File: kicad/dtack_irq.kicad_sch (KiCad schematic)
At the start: 14 parts, among them U12 GAL22V10, U13 GAL22V10

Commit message: - Added buffers for LED indicators in kicad - Removed pullups on FC0.2 in kicad - Connected FC0-2 to glue logic in kicad - Revamped glue logic for irg and iack in Digital
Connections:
- net ~{IACK6} is gone; now on net ~{IACK1}: U13.15 (I/O)
- net ~{IACK1}: no longer U13.19 (I/O)
- net ~{IACK2}: now also U13.16 (I/O); no longer U13.18 (I/O)
- net ~{IACK3}: now also U13.17 (I/O); no longer U13.21 (I/O)
- net ~{IACK4}: now also U13.18 (I/O); no longer U13.17 (I/O)
- net ~{IACK5}: now also U13.19 (I/O), U13.20 (I/O); no longer U13.16 (I/O)
- net ~{IACK7}: now also U13.21 (I/O); no longer U13.14 (I/O)
- no-connect marks 0 -> 14
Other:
- note added: "Pin 14 is IACK0. Never connect to ground!"
- title: (none) -> Mats Brorson 68010 SBC DTACK and IRQ
- moved on the sheet: JP1, R8, R?, U12, U13

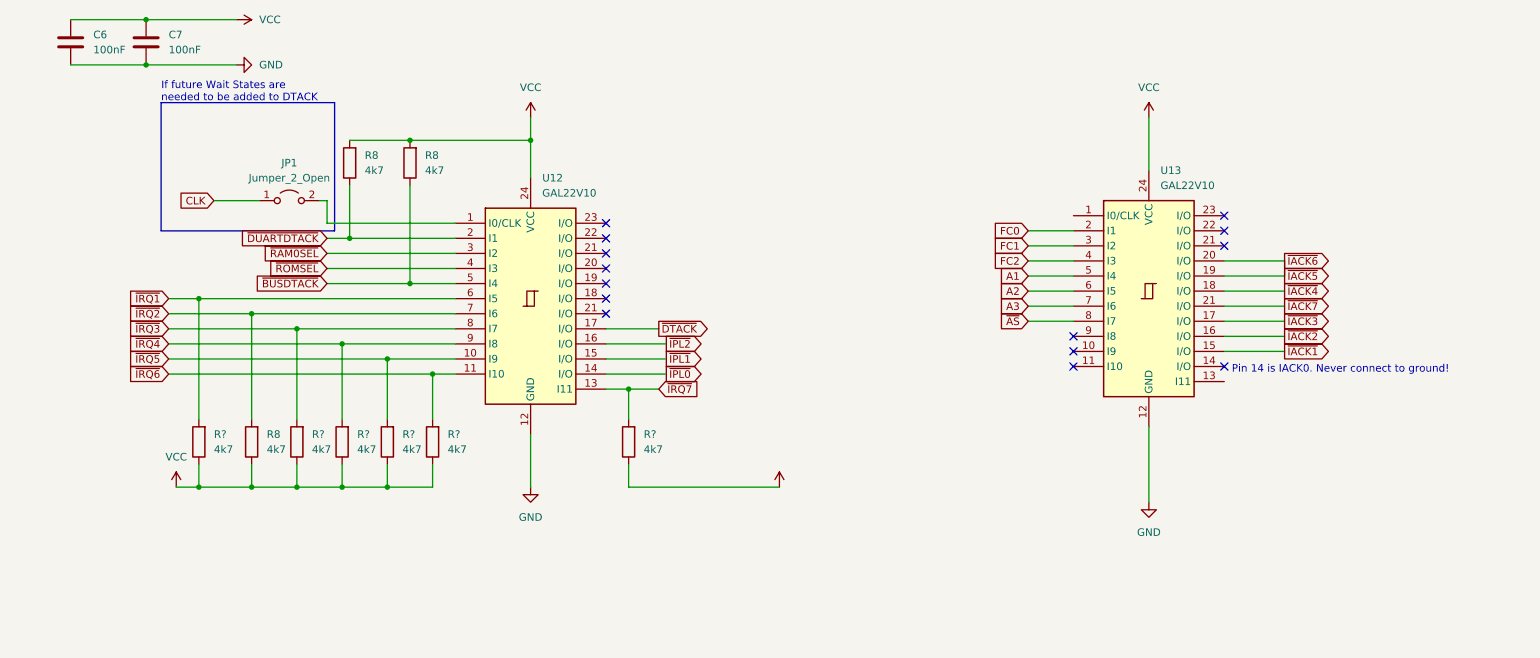
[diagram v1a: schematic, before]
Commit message: New decoding and GALs
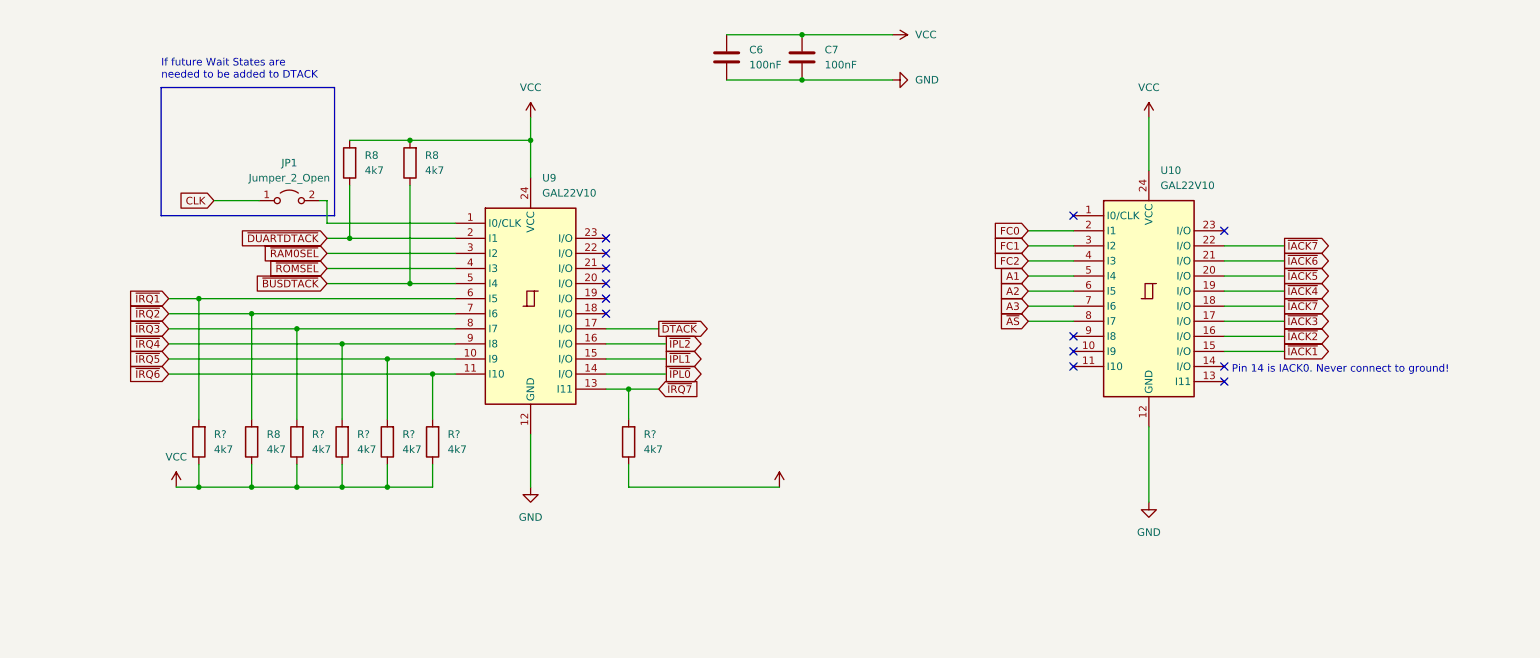
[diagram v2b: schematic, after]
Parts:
- removed U12, U13: GAL22V10, symbol Lattice_GAL_sym:GAL22V10
- added U10, U9: GAL22V10, symbol Lattice_GAL_sym:GAL22V10
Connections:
- net A1: now also U10.5 (I4)
- net A2: now also U10.6 (I5)
- net A3: now also U10.7 (I6)
- net FC0: now also U10.2 (I1)
- net FC1: now also U10.3 (I2)
- net FC2: now also U10.4 (I3)
- net GND: now also U10.12 (GND), U9.12 (GND)
- net VCC: now also U10.24 (VCC), U9.24 (VCC)
- net ~{AS}: now also U10.8 (I7)
- net ~{BUSDTACK}: now also U9.5 (I4)
- net ~{DTACK}: now also U9.17 (I/O)
- net ~{DUARTDTACK}: now also U9.2 (I1)
- net ~{IACK1}: now also U10.15 (I/O)
- net ~{IACK2}: now also U10.16 (I/O)
- net ~{IACK3}: now also U10.17 (I/O)
- net ~{IACK4}: now also U10.19 (I/O)
- net ~{IACK5}: now also U10.20 (I/O)
- net ~{IACK7}: now also U10.18 (I/O), U10.22 (I/O)
- net ~{IPL0}: now also U9.14 (I/O)
- net ~{IPL1}: now also U9.15 (I/O)
- net ~{IPL2}: now also U9.16 (I/O)
- net ~{IRQ1}: now also U9.6 (I5)
- net ~{IRQ2}: now also U9.7 (I6)
- net ~{IRQ3}: now also U9.8 (I7)
- net ~{IRQ4}: now also U9.9 (I8)
- net ~{IRQ5}: now also U9.10 (I9)
- net ~{IRQ6}: now also U9.11 (I10)
- net ~{IRQ7}: now also U9.13 (I11)
- net ~{RAM0SEL}: now also U9.3 (I2)
- net ~{ROMSEL}: now also U9.4 (I3)
- net at JP1.2 (B): now also U9.1 (I0/CLK)
- new net ~{IACK6}: U10.21 (I/O)
- no-connect marks 14 -> 13
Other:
- moved on the sheet: C6, C7

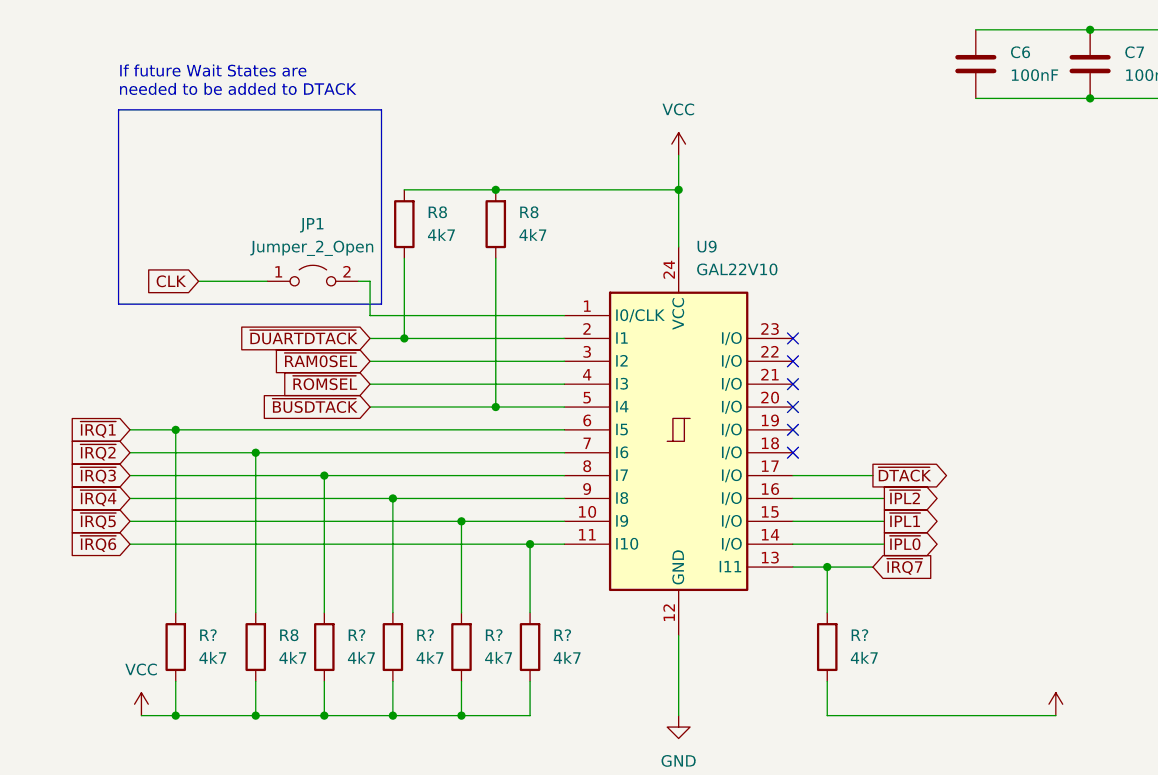
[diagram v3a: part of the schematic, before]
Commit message: switched to GALasm
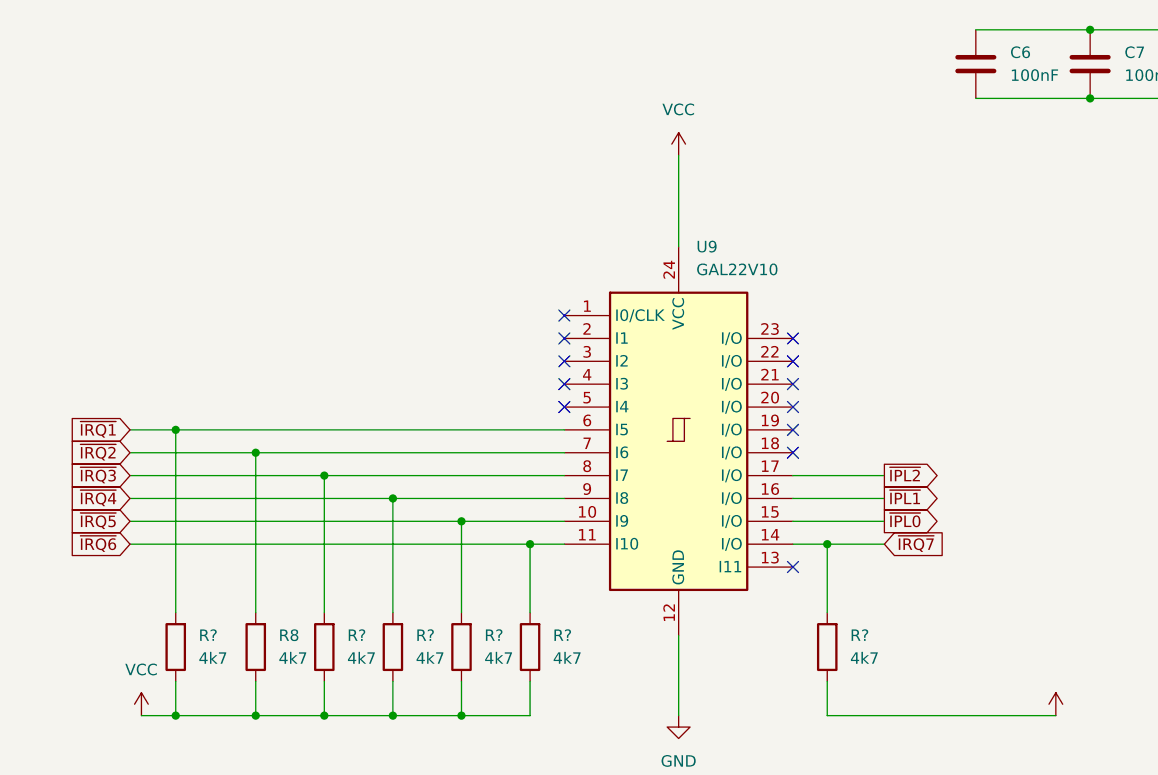
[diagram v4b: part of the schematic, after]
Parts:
- removed JP1: Jumper_2_Open, symbol Jumper:Jumper_2_Open
- removed R8 (x2): 4k7, Resistor_THT:R_Axial_DIN0207_L6.3mm_D2.5mm_P10.16mm_Horizontal, symbol Device:R
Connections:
- net ~{DTACK} is gone; now on net ~{IPL2}: U9.17 (I/O)
- net ~{IPL0}: now also U9.15 (I/O); no longer U9.14 (I/O)
- net ~{IPL1}: now also U9.16 (I/O); no longer U9.15 (I/O)
- net ~{IPL2}: no longer U9.16 (I/O)
- net ~{IRQ7}: now also U9.14 (I/O); no longer U9.13 (I11)
- net ~{BUSDTACK}: no longer names the net of U9.5 (I4)
- net ~{DUARTDTACK}: no longer names the net of U9.2 (I1)
- net ~{RAM0SEL}: no longer names the net of U9.3 (I2)
- net ~{ROMSEL}: no longer names the net of U9.4 (I3)
- no-connect marks 13 -> 19
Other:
- note removed: "If future Wait States are needed to be added to DTACK"

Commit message: finalized signaling PLD
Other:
- title: Mats Brorson 68010 SBC DTACK and IRQ -> Mats Brorson 68010 SBC IACK and IRQ
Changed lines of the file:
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@@
   (paper "A4")
   (title_block
-    (title "Mats Brorson 68010 SBC DTACK and IRQ")
+    (title "Mats Brorson 68010 SBC IACK and IRQ")
     (date "2023-12-28")
     (rev "1.0-alpha")

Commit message: added footprints
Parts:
- added J10, J14, J15, J9: Free pin, Connector_PinSocket_2.54mm:PinSocket_1x01_P2.54mm_Vertical, symbol Connector:Conn_01x01_Pin
- added J11: Free Pins, Connector_PinSocket_2.54mm:PinSocket_1x05_P2.54mm_Vertical, symbol Connector:Conn_01x05_Pin
- added J12: Free pins, Connector_PinSocket_2.54mm:PinSocket_1x06_P2.54mm_Vertical, symbol Connector:Conn_01x06_Pin
- added J13: Free pins, Connector_PinSocket_2.54mm:PinSocket_1x03_P2.54mm_Vertical, symbol Connector:Conn_01x03_Pin
- U16: renamed from U10; footprint (none) -> Package_DIP:DIP-24_W7.62mm_Socket
- U17: renamed from U9; footprint (none) -> Package_DIP:DIP-24_W7.62mm_Socket
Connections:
- net at U16.1 (I0/CLK): now also J9.1 (Pin_1)
- net at U16.10 (I9): now also J13.2 (Pin_2)
- net at U16.11 (I10): now also J13.3 (Pin_3)
- net at U16.13 (I11): now also J14.1 (Pin_1)
- net at U16.23 (I/O): now also J10.1 (Pin_1)
- net at U16.9 (I8): now also J13.1 (Pin_1)
- net at U17.1 (I0/CLK): now also J11.1 (Pin_1)
- net at U17.13 (I11): now also J15.1 (Pin_1)
- net at U17.18 (I/O): now also J12.6 (Pin_6)
- net at U17.19 (I/O): now also J12.5 (Pin_5)
- net at U17.2 (I1): now also J11.2 (Pin_2)
- net at U17.20 (I/O): now also J12.4 (Pin_4)
- net at U17.21 (I/O): now also J12.3 (Pin_3)
- net at U17.22 (I/O): now also J12.2 (Pin_2)
- net at U17.23 (I/O): now also J12.1 (Pin_1)
- net at U17.3 (I2): now also J11.3 (Pin_3)
- net at U17.4 (I3): now also J11.4 (Pin_4)
- net at U17.5 (I4): now also J11.5 (Pin_5)
- no-connect marks 19 -> 1

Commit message: saving state
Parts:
- C6, C7: footprint Capacitor_THT:CP_Radial_D5.0mm_P2.50mm -> Capacitor_THT:C_Disc_D5.0mm_W2.5mm_P2.50mm
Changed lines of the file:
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@@
       (effects (font (size 1.27 1.27)) (justify left))
     )
-    (property "Footprint" "Capacitor_THT:CP_Radial_D5.0mm_P2.50mm" (at 143.2052 26.67 0)
+    (property "Footprint" "Capacitor_THT:C_Disc_D5.0mm_W2.5mm_P2.50mm" (at 143.2052 26.67 0)
       (effects (font (size 1.27 1.27)) hide)
     )
@@
       (effects (font (size 1.27 1.27)) (justify left))
     )
-    (property "Footprint" "Capacitor_THT:CP_Radial_D5.0mm_P2.50mm" (at 130.5052 26.67 0)
-      (effects (font (size 1.27 1.27)) hide)
-    )
+    (property "Footprint" "Capacitor_THT:C_Disc_D5.0mm_W2.5mm_P2.50mm" (at 130.5052 26.67 0)
+      (effects (font (size 1.27 1.27)) hide)
+    )
